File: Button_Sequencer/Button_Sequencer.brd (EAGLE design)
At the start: 153.7 x 103.8 mm, 85 parts, among them IC1 OPA2134P

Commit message: fixed power
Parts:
- moved C16 1.27 mm to (109.2, 26.7)
- moved R16 1.27 mm to (114.3, 26.7)
- moved VR16 1.27 mm to (120.7, 26.7)
- moved C17 1.27 mm to (109.2, 16.5)
- moved R17 1.27 mm to (114.3, 16.5)
- moved VR17 1.27 mm to (120.7, 16.5)
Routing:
- net TEENSY_L: track 0.00 -> 33.3 mm
- net TEENSY_R: track 0.00 -> 10.2 mm
- net +5V: track 224.6 -> 227.3 mm
- net N$4: track 4.76 -> 2.86 mm
- net L_INPUT8: track 33.3 -> 33.9 mm
- net L_INPUT7: track 33.3 -> 33.9 mm
- net +3V3: track 123.2 -> 123.1 mm, vias 0 -> 1

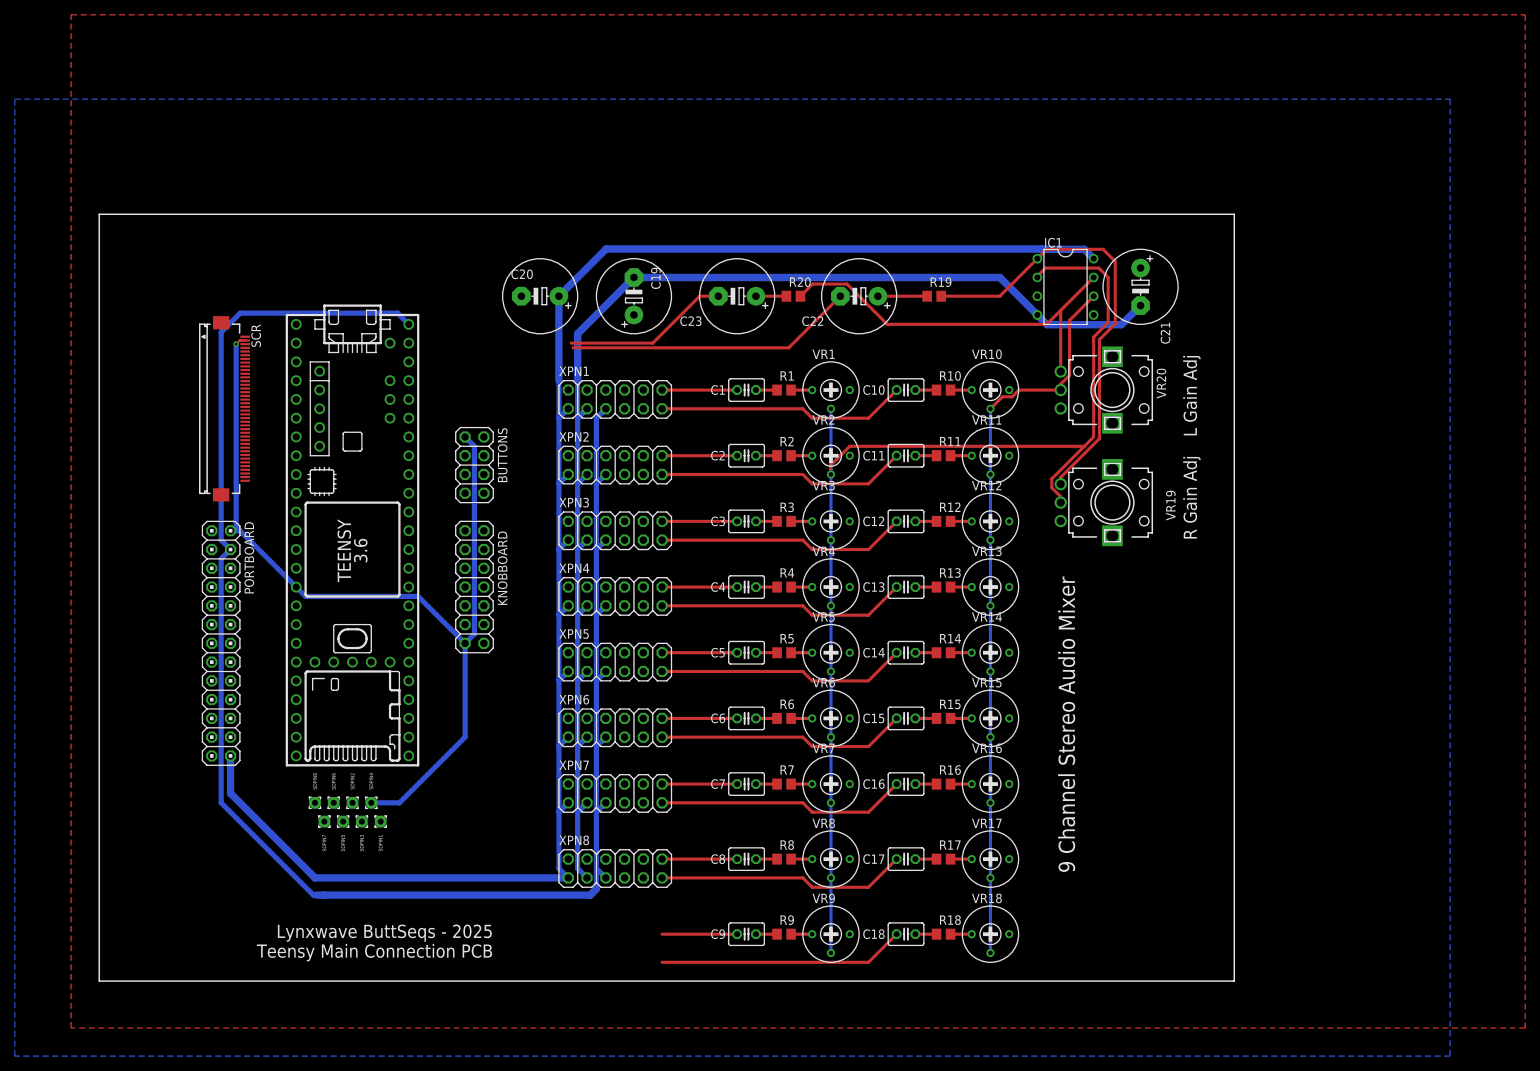
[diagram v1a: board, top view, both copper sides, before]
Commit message: Fixed lost commit from merger
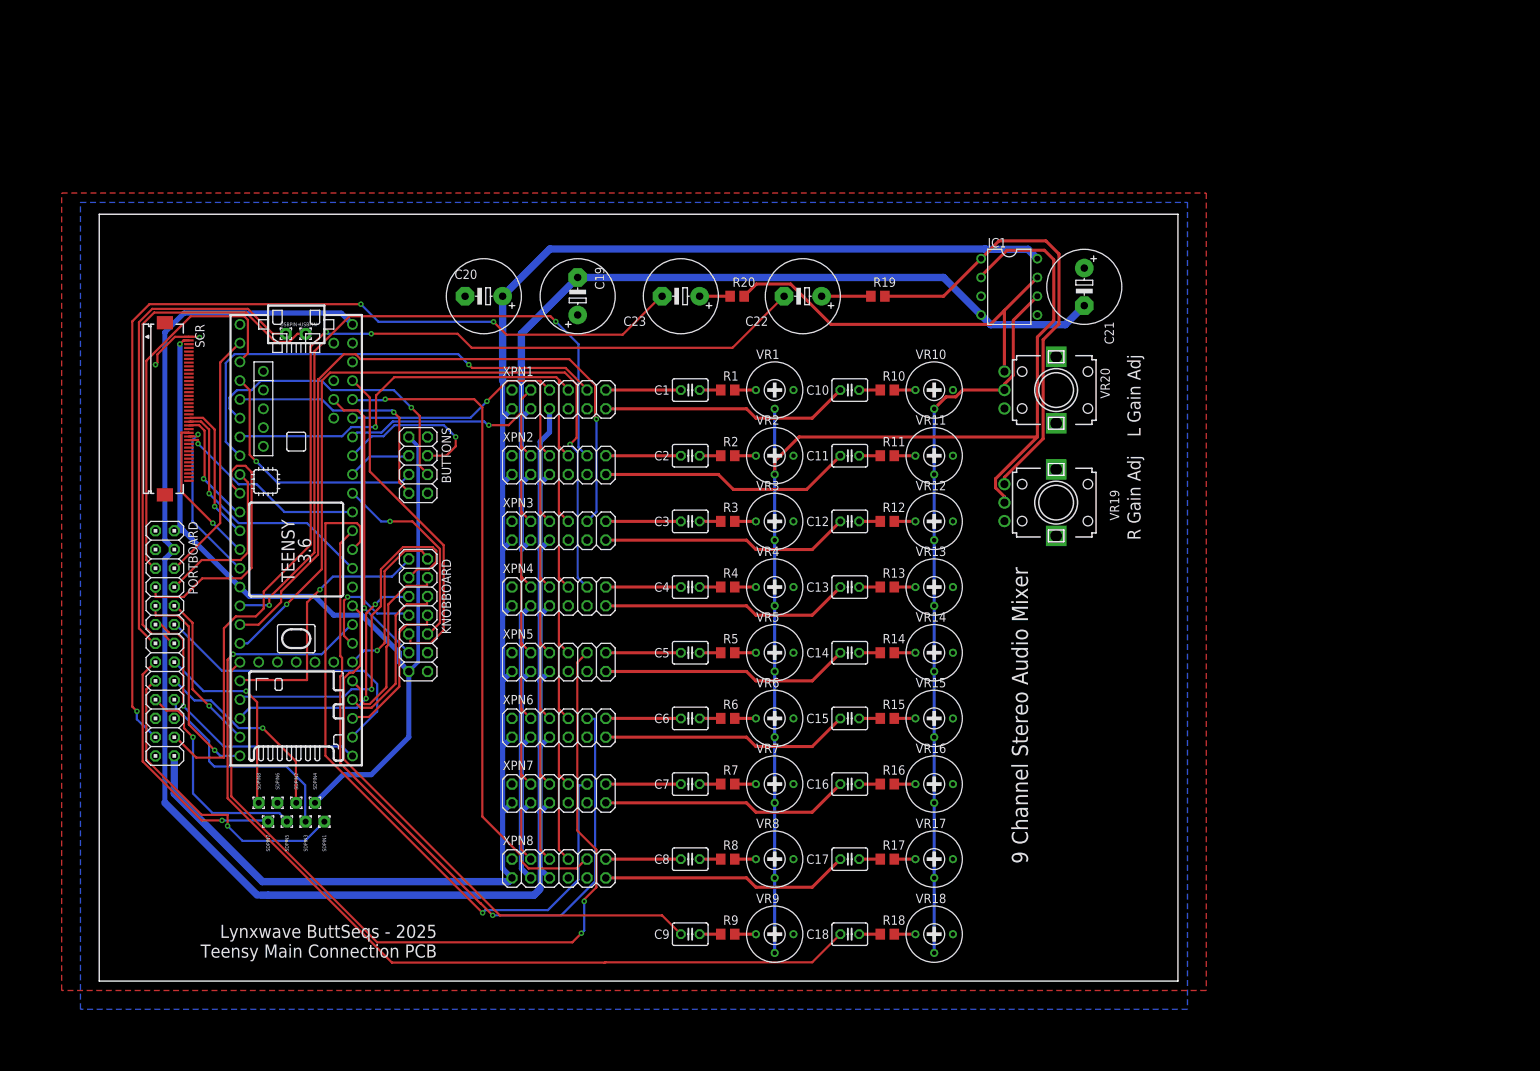
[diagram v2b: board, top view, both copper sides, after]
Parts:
- added USBPIN+, USBPIN-: (no value), wirepad:1,6/0,8
- moved KNOBBOARD 8.52 mm to (43.2, 49.5)
- moved C10 7.62 mm to (101.6, 80.0)
- moved C11 7.62 mm to (101.6, 71.1)
- moved C12 7.62 mm to (101.6, 62.2)
- moved C13 7.62 mm to (101.6, 53.3)
- moved C14 7.62 mm to (101.6, 44.5)
- moved C15 7.62 mm to (101.6, 35.6)
- moved C16 7.62 mm to (101.6, 26.7)
- moved C17 7.62 mm to (101.6, 16.5)
- moved C18 7.62 mm to (101.6, 6.35)
- moved C19 7.62 mm to (64.8, 92.7)
- moved C21 7.62 mm to (133.3, 94.0)
- moved C22 7.62 mm to (95.2, 92.7)
- moved C23 7.62 mm to (78.7, 92.7)
- moved IC1 7.62 mm to (123.2, 94.0)
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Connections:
- net USBDATA+: now also USBPIN+.1; no longer TEENSY_3.6.UD+
- net USBDATA-: now also USBPIN-.1; no longer TEENSY_3.6.UD-
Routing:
- net XPN_MISO: track 0.00 -> 127.3 mm, vias 0 -> 1
- net XPN_CS5: track 0.00 -> 115.2 mm, vias 0 -> 2
- net OUTPUT_L: track 22.6 -> 134.2 mm, vias 0 -> 3
- net XPN_MOSI: track 0.00 -> 105.4 mm, vias 0 -> 1
- net XPN_CS4: track 0.00 -> 105.1 mm, vias 0 -> 2
- net XPN_CLK: track 0.00 -> 101.3 mm, vias 0 -> 1
- net XPN_CS6: track 0.00 -> 100.4 mm, vias 0 -> 1
- net OUTPUT_R: track 39.1 -> 138.7 mm, vias 0 -> 2
- net XPN_CS3: track 0.00 -> 99.1 mm, vias 0 -> 1
- net XPN_CS7: track 0.00 -> 98.9 mm, vias 0 -> 1
- net TEENSY_L: track 33.3 -> 131.4 mm, vias 0 -> 1
- net XPN_CS2: track 0.00 -> 95.8 mm, vias 0 -> 2
- net XPN_CS8: track 0.00 -> 91.6 mm, vias 0 -> 1
- net USBDATA-: track 0.00 -> 71.3 mm
- net TEENSY_R: track 10.2 -> 77.9 mm
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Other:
- board size 153.7 x 103.8 mm -> 146 x 103.8 mm

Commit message: Added +-12V barrel connetor TODO single +12V supply varient
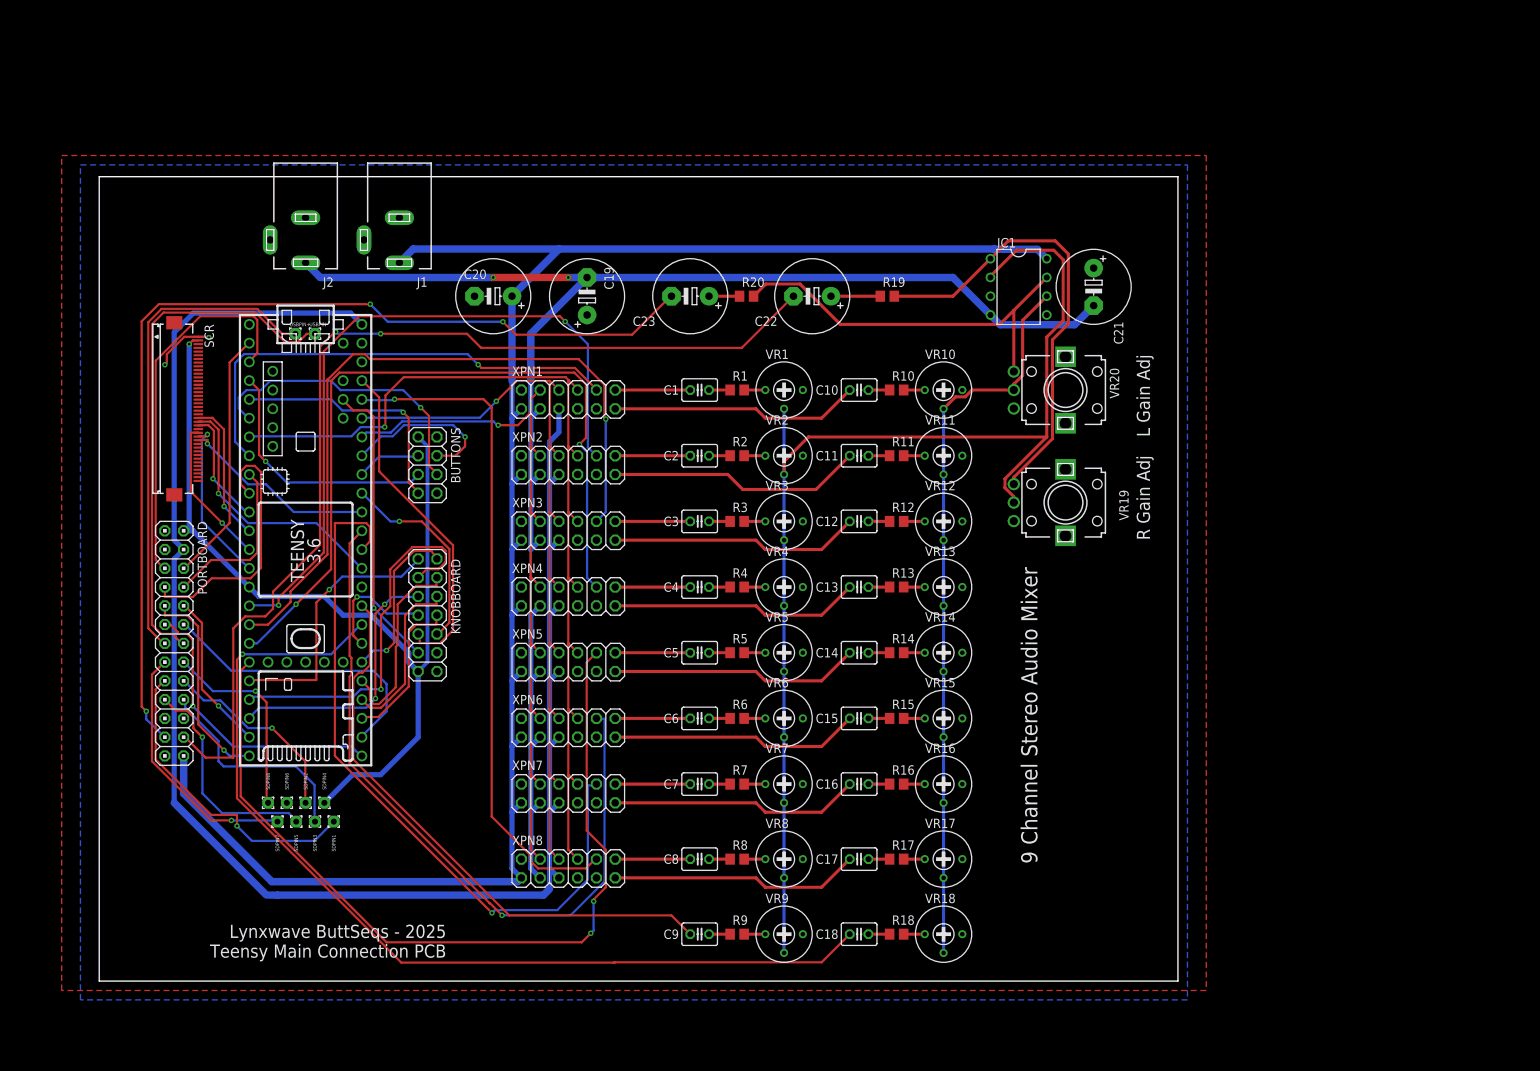
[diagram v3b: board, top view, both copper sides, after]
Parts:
- added J1, J2: DCJ0202, con-jack:DCJ0202
- moved C10 1.27 mm to (102.9, 80.0)
- moved C11 1.27 mm to (102.9, 71.1)
- moved C12 1.27 mm to (102.9, 62.2)
- moved C13 1.27 mm to (102.9, 53.3)
- moved C14 1.27 mm to (102.9, 44.5)
- moved C15 1.27 mm to (102.9, 35.6)
- moved C16 1.27 mm to (102.9, 26.7)
- moved C17 1.27 mm to (102.9, 16.5)
- moved C18 1.27 mm to (102.9, 6.35)
- moved C19 1.27 mm to (66.0, 92.7)
- moved C21 1.27 mm to (134.6, 94.0)
- moved C23 1.27 mm to (80.0, 92.7)
- moved R19 1.27 mm to (106.7, 92.7)
- moved VR19 1.27 mm to (130.8, 64.8)
- moved VR20 1.27 mm to (130.8, 80.0)
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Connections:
- net +12V: now also J1.1
- net -12V: now also J2.1
- net GND: now also J1.3, J2.3
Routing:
- net -12V: track 169.8 -> 208.8 mm, vias 0 -> 2
- net +12V: track 223.4 -> 245.8 mm
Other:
- board size 146 x 103.8 mm -> 146 x 108.9 mm
